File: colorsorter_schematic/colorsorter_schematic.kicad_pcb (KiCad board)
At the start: 2 copper layers, 6 parts, among them U1 PIC24FJ64GA702-I/SO, U2 ESP8266-01_ESP-01

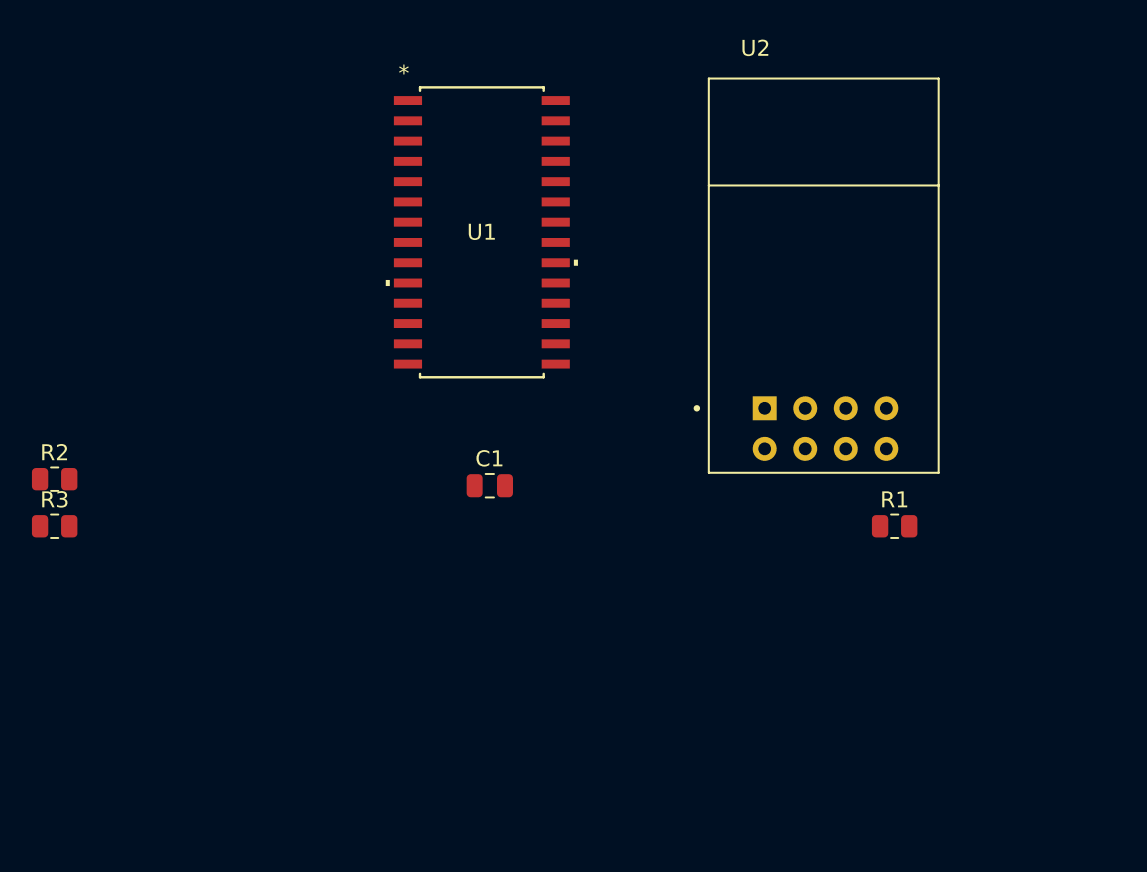
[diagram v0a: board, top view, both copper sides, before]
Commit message: Added voltage regulator, oscillator and bulk capacitors.
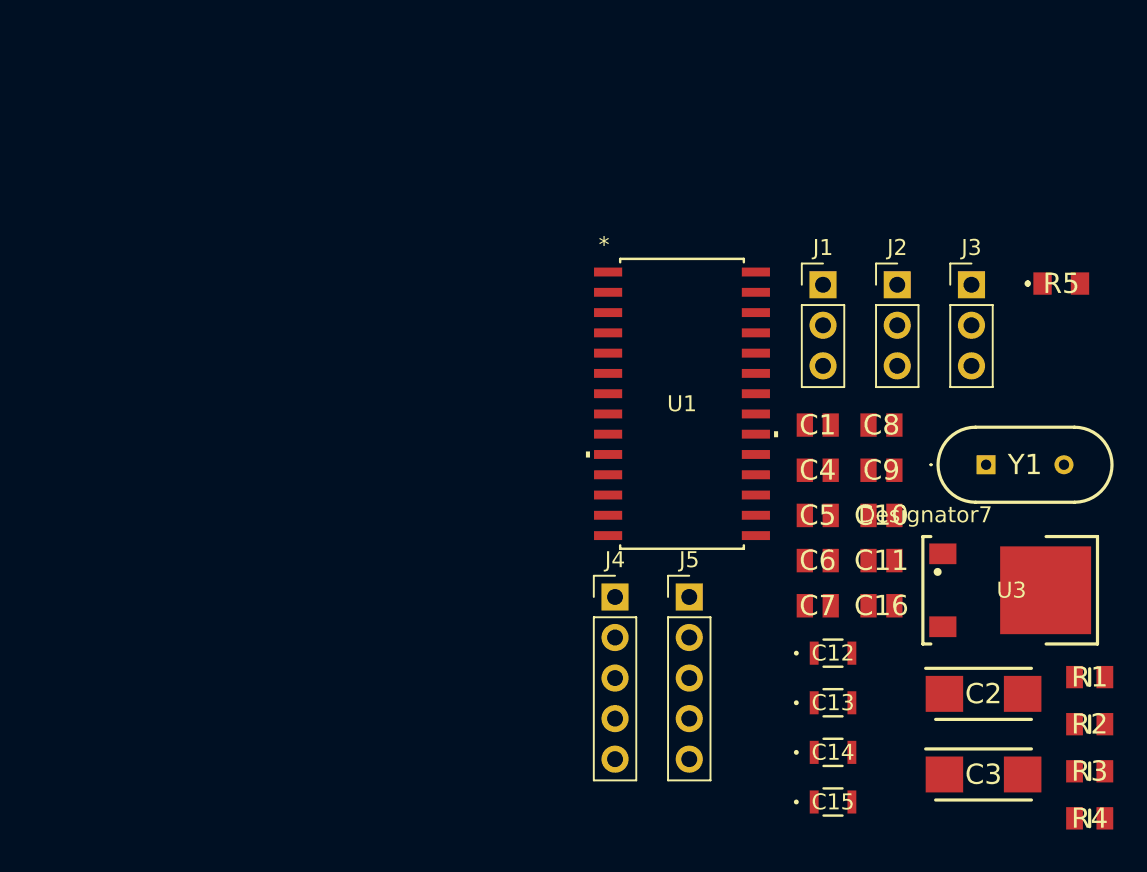
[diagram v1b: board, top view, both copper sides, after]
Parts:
- removed U2: ESP8266-01_ESP-01, ESP8266-01_ESP-01:XCVR_ESP8266-01_ESP-01
- added C10: 0.1u, 0.1uF:CAPC2012X94N, F.Cu at (122.0, 75.5)
- added C11: 0.1u, 0.1uF:CAPC2012X94N, F.Cu at (122.0, 78.3)
- added C12: 10u, 10uF:CAP_2012_TDK, F.Cu at (119.0, 84.1)
- added C13: 10u, 10uF:CAP_2012_TDK, F.Cu at (119.0, 87.3)
- added C14: 10u, 10uF:CAP_2012_TDK, F.Cu at (119.0, 90.4)
- added C15: 10u, 10uF:CAP_2012_TDK, F.Cu at (119.0, 93.5)
- added C16: 0.1u, 0.1uF:CAPC2012X94N, F.Cu at (122.0, 81.2)
- added C2: 10u, 10uFtantalum:CAPPM6032X280N, F.Cu at (128.4, 86.7)
- added C3: 10u, 10uFtantalum:CAPPM6032X280N, F.Cu at (128.4, 91.8)
- added C4: 50p, 50pF:CAPC2012X140N, F.Cu at (118.0, 72.7)
- added C5: 50p, 50pF:CAPC2012X140N, F.Cu at (118.0, 75.5)
- added C6: 0.1u, 0.1uF:CAPC2012X94N, F.Cu at (118.0, 78.3)
- added C7: 0.1u, 0.1uF:CAPC2012X94N, F.Cu at (118.0, 81.2)
- added C8: 0.1u, 0.1uF:CAPC2012X94N, F.Cu at (122.0, 69.9)
- added C9: 0.1u, 0.1uF:CAPC2012X94N, F.Cu at (122.0, 72.7)
- added J1: Conn_01x03_Pin, Connector_PinHeader_2.54mm:PinHeader_1x03_P2.54mm_Vertical, F.Cu at (118.3, 61.1)
- added J2: Conn_01x03_Pin, Connector_PinHeader_2.54mm:PinHeader_1x03_P2.54mm_Vertical, F.Cu at (123.0, 61.1)
- added J3: Conn_01x03_Pin, Connector_PinHeader_2.54mm:PinHeader_1x03_P2.54mm_Vertical, F.Cu at (127.6, 61.1)
- added J4: Conn_01x05_Pin, Connector_PinHeader_2.54mm:PinHeader_1x05_P2.54mm_Vertical, F.Cu at (105.3, 80.6)
- added J5: Conn_01x05_Pin, Connector_PinHeader_2.54mm:PinHeader_1x05_P2.54mm_Vertical, F.Cu at (110.0, 80.6)
- added R4: 10k, 10kohm:RESC2012X70N, F.Cu at (135.1, 94.5)
- added R5: 330, 330ohm:ERJP06D1000V, F.Cu at (133.3, 61.0)
- added U3: LM1117DT-3.3/NOPB, voltageregulator:NDP0003B, F.Cu at (130.2, 80.2)
- added Y1: 830003156B, crystaloscillator:830003156B, F.Cu at (128.6, 72.3)
- C1: value 100n -> 0.1u; footprint capacitor_smd:C_0805_2012Metric -> 0.1uF:CAPC2012X94N
- R1: footprint Resistor_SMD:R_0805_2012Metric -> 10kohm:RESC2012X70N
- R2, R3: value 4.7k -> 10k; footprint Resistor_SMD:R_0805_2012Metric -> 10kohm:RESC2012X70N
- U1: footprint footprints:SOIC28__SO28_MCH -> PIC24FJ64GA702-I-SO:SOIC28__SO28_MCH
- moved R2 66.6 mm to (135.1, 88.6)
- moved R3 66.6 mm to (135.1, 91.5)
- moved C1 20.9 mm to (118.0, 69.9)
- moved U1 16.5 mm to (109.5, 68.5)
- moved R1 15.4 mm to (135.1, 85.7)
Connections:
- C1 pad 1: +3.3V -> Net-(U2-GND)
- C1 pad 2: GND -> +3.3V
- R1 pad 1: Net-(U2-~{RST}) -> +3.3V
- R1 pad 2: +3.3V -> Net-(U2-~{RST})
- R2 pad 1: +3.3V -> Net-(J4-Pin_3)
- R2 pad 2: Net-(SDA1-Pin_1) -> GND
- R3 pad 1: +3.3V -> Net-(J4-Pin_4)
- R3 pad 2: Net-(SCL1-Pin_1) -> GND
- U1 pad 1: unconnected-(U1-*MCLR-Pad1) -> Net-(SW1-B)
- U1 pad 10: unconnected-(U1-OSCO/CLKO/C2IND/RA3-Pad10) -> Net-(U1-OSCO/CLKO/C2IND/RA3)
- U1 pad 13: unconnected-(U1-VDD-Pad13) -> +3.3V
- U1 pad 14: unconnected-(U1-PGD3/RP5/ASDA1/OCM1E/RB5-Pad14) -> Net-(J2-Pin_3)
- U1 pad 17: Net-(SCL1-Pin_1) -> /SCL
- U1 pad 18: Net-(SDA1-Pin_1) -> /SDA
- U1 pad 19: unconnected-(U1-VSS-Pad19) -> GND
- U1 pad 20: unconnected-(U1-VCAP-Pad20) -> Net-(U1-VCAP)
- U1 pad 25: unconnected-(U1-CVREF/AN6/C3INB/RP14/CTED5/RB14-Pad25) -> Net-(J3-Pin_3)
- U1 pad 26: unconnected-(U1-AN9/C3INA/RP15/CTED6/RB15-Pad26) -> Net-(J1-Pin_3)
- U1 pad 27: unconnected-(U1-AVSS/VSS-Pad27) -> GND
- U1 pad 28: unconnected-(U1-AVDD/VDD-Pad28) -> +3.3V
- U1 pad 4: unconnected-(U1-PGD1/AN2/CTCMP/C2INB/RP0/RB0-Pad4) -> Net-(J4-Pin_3)
- U1 pad 5: unconnected-(U1-PGC1/AN1-/AN3/C2INA/RP1/CTED12/RB1-Pad5) -> Net-(J4-Pin_4)
- U1 pad 8: unconnected-(U1-VSS-Pad8) -> GND
- U1 pad 9: unconnected-(U1-OSCI/CLKI/C1IND/RA2-Pad9) -> Net-(U1-OSCI/CLKI/C1IND/RA2)

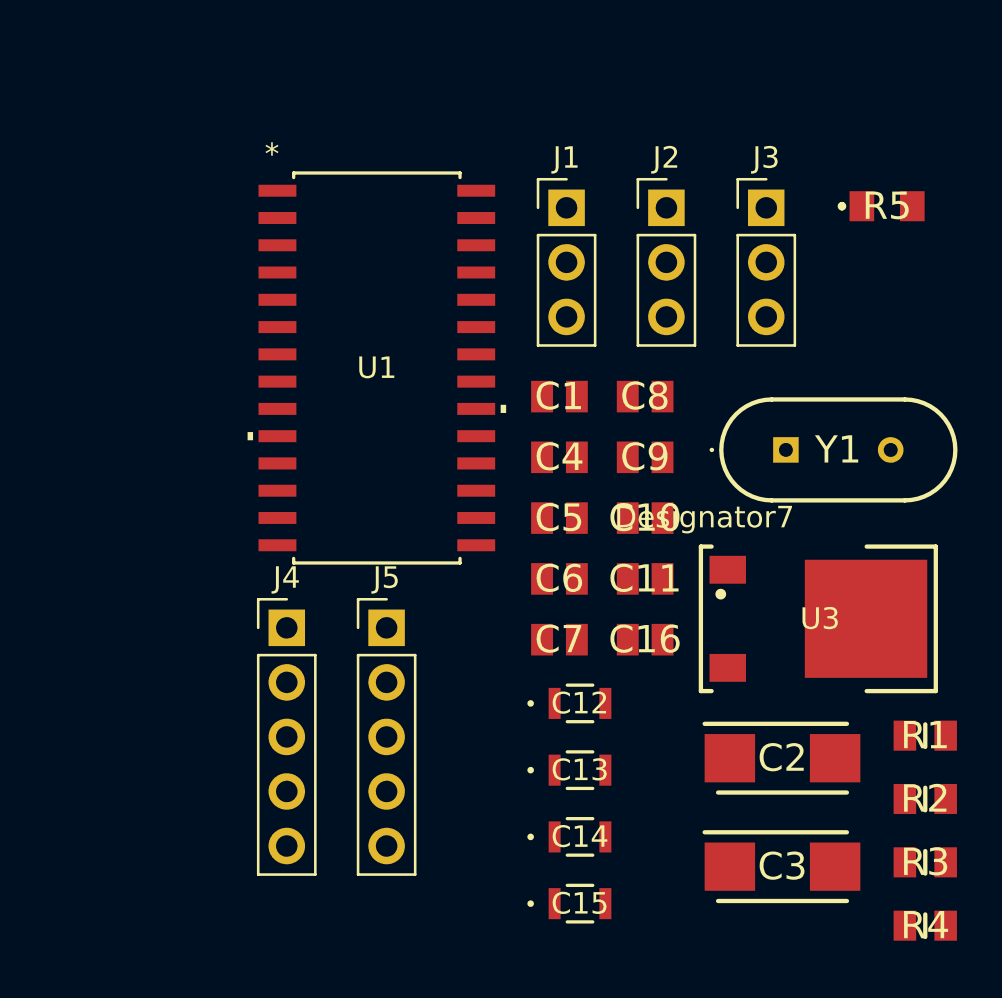
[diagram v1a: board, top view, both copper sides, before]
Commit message: Added additional pins header.
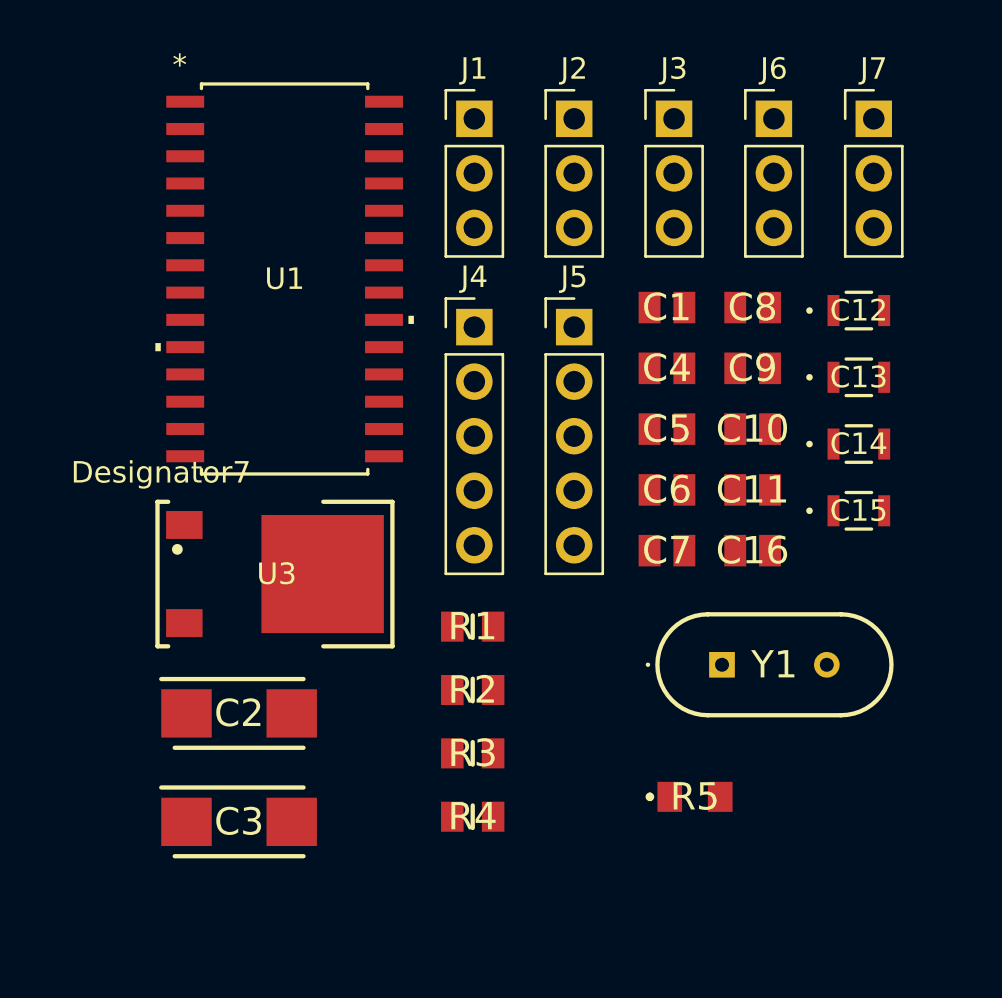
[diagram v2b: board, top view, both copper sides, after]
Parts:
- added J6: Conn_01x03_Pin, Connector_PinHeader_2.54mm:PinHeader_1x03_P2.54mm_Vertical, F.Cu at (128.0, 56.9)
- added J7: Conn_01x03_Pin, Connector_PinHeader_2.54mm:PinHeader_1x03_P2.54mm_Vertical, F.Cu at (132.7, 56.9)
- moved R5 28.9 mm to (124.3, 88.5)
- moved C2 25.4 mm to (103.1, 84.6)
- moved C3 25.4 mm to (103.1, 89.7)
- moved U3 25.4 mm to (104.8, 78.1)
- moved C12 22.4 mm to (132.0, 65.9)
- moved C13 22.4 mm to (132.0, 69.0)
- moved C14 22.4 mm to (132.0, 72.1)
- moved C15 22.4 mm to (132.0, 75.2)
- moved R1 21.7 mm to (114.0, 80.6)
- moved R3 21.7 mm to (114.0, 86.5)
- moved R4 21.7 mm to (114.0, 89.4)
- moved R2 21.7 mm to (114.0, 83.5)
- moved J4 16.5 mm to (114.0, 66.6)
- moved J5 16.5 mm to (118.7, 66.6)
- moved Y1 10.4 mm to (125.6, 82.3)
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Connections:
- C1 pad 1: Net-(U2-GND) -> GND
- U1 pad 11: unconnected-(U1-SOSCI/RP4/RB4-Pad11) -> Net-(J7-Pin_3)
- U1 pad 22: unconnected-(U1-PGC2/TMS/REFI1/RP11/CTED9/RB11-Pad22) -> Net-(J6-Pin_3)
- U1 pad 23: unconnected-(U1-AN8/LVDIN/RP12/RB12-Pad23) -> Net-(J6-Pin_2)
- U1 pad 24: unconnected-(U1-AN7/C1INC/RP13/OCM1D/CTPLS/RB13-Pad24) -> Net-(J6-Pin_1)
- U1 pad 6: unconnected-(U1-AN4/C1INB/RP2/SDA2/CTED13/RB2-Pad6) -> Net-(J7-Pin_1)
- U1 pad 7: unconnected-(U1-AN5/C1INA/RP3/SCL2/CTED8/RB3-Pad7) -> Net-(J7-Pin_2)

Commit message: Dodavanje izmjena u semi i rutranje na pcb
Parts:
- added Power: PinHeader_1x02_P2.54mm_Vertical, Connector_PinHeader_2.54mm:PinHeader_1x02_P2.54mm_Vertical, F.Cu at (61.0, 86.4)
- added REF**: XCVR_ESP8266-01_ESP-01, ESP8266-01_ESP-01 FOOTPRINT:XCVR_ESP8266-01_ESP-01, F.Cu at (122.9, 91.9)
- added S**: SLW12768644AD, SwitcH:SLW12768644AD, F.Cu at (77.5, 44.8)
- moved R5 68.0 mm to (68.6, 49.5)
- moved R4 66.6 mm to (63.5, 46.0), turned to -90 degrees
- moved C6 63.5 mm to (63.5, 52.1), turned to 90 degrees
- moved C7 53.4 mm to (72.0, 92.7)
- moved J4 50.7 mm to (63.5, 62.2)
- moved R3 45.8 mm to (70.8, 71.1)
- moved R2 45.8 mm to (71.1, 67.3)
- moved C4 44.6 mm to (78.5, 66.3), turned to 180 degrees
- moved C5 44.1 mm to (78.9, 70.0), turned to 180 degrees
- moved C14 43.8 mm to (88.9, 80.2), turned to 90 degrees
- moved C8 43.3 mm to (90.2, 88.4), turned to 90 degrees
- moved Y1 42.6 mm to (84.8, 70.0), turned to 90 degrees
- moved C9 38.8 mm to (88.9, 76.0), turned to 90 degrees
- moved J7 38.4 mm to (95.3, 48.3), turned to 90 degrees
- moved C1 36.5 mm to (105.6, 97.8), turned to 180 degrees
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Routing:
- net GND: track 0.00 -> 39.6 mm, vias 0 -> 2
- net +3.3V: track 0.00 -> 35.5 mm
- net (no net): track 0.00 -> 32.9 mm
- net Net-(J6-Pin_1): track 0.00 -> 20.7 mm
- net Net-(J6-Pin_2): track 0.00 -> 17.9 mm
- net Net-(J7-Pin_2): track 0.00 -> 17.8 mm
- net Net-(SW1-B): track 0.00 -> 14.5 mm
- net Net-(U1-OSCI/CLKI/C1IND/RA2): track 0.00 -> 14.0 mm
- net Net-(J6-Pin_3): track 0.00 -> 14.0 mm
- net Net-(SW1-A): track 0.00 -> 9.59 mm
- net +4.5V: track 0.00 -> 8.65 mm
- net Net-(C6-Pad2): track 0.00 -> 8.49 mm
- net Net-(J4-Pin_4): track 0.00 -> 8.40 mm
- net Net-(U1-OSCO/CLKO/C2IND/RA3): track 0.00 -> 7.04 mm
- net Net-(U1-VCAP): track 0.00 -> 3.78 mm
- added copper zone on B.Cu, net GND

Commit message: Updated schematic and pcb.
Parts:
- removed Power: PinHeader_1x02_P2.54mm_Vertical, Connector_PinHeader_2.54mm:PinHeader_1x02_P2.54mm_Vertical
- removed REF**: XCVR_ESP8266-01_ESP-01, ESP8266-01_ESP-01 FOOTPRINT:XCVR_ESP8266-01_ESP-01
- removed S**: SLW12768644AD, SwitcH:SLW12768644AD
- added J8: Conn_01x02_Pin, Connector_PinHeader_2.54mm:PinHeader_1x02_P2.54mm_Vertical, F.Cu at (166.1, 97.1)
- added SW1: SW_SPDT, twostateswitch:SLW12768644AD, F.Cu at (145.9, 107.5)
- added U2: ESP8266-01_ESP-01, wifi:wifi, F.Cu at (134.9, 86.4)
- U3: footprint voltageregulator:NDP0003B -> NDP0003B:NDP0003B
- moved R4 112.8 mm to (166.0, 93.3), turned to 0 degrees
- moved J4 106.3 mm to (160.8, 104.8)
- moved R5 103.3 mm to (159.1, 99.4)
- moved C6 102.7 mm to (157.8, 92.9), turned to 0 degrees
- moved R3 97.1 mm to (166.0, 90.3)
- moved R2 97.0 mm to (166.0, 87.4)
- moved C7 85.8 mm to (157.8, 95.7)
- moved C4 82.0 mm to (157.8, 87.2), turned to 0 degrees
- moved C5 81.3 mm to (157.8, 90.0), turned to 0 degrees
- moved Y1 77.7 mm to (147.3, 116.3), turned to 0 degrees
- moved C9 73.7 mm to (161.7, 87.2), turned to 0 degrees
- moved J7 73.6 mm to (163.7, 75.6), turned to 0 degrees
- moved C8 71.7 mm to (161.7, 84.4), turned to 0 degrees
- moved C10 66.9 mm to (161.7, 90.0), turned to 0 degrees
- moved C13 66.6 mm to (137.9, 112.1)
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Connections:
- net +3.3V renamed Net-(C3-+)
- net +4.5V renamed Net-(C2-+)
- Y1 pad 1: (no net) -> Net-(U1-OSCO/CLKO/C2IND/RA3)
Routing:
- net GND: track 39.6 -> 0.00 mm, vias 2 -> 0
- net Net-(C3-+): track 35.5 -> 0.00 mm
- net (no net): track 32.9 -> 0.00 mm
- net Net-(J6-Pin_1): track 20.7 -> 0.00 mm
- net Net-(J6-Pin_2): track 17.9 -> 0.00 mm
- net Net-(J7-Pin_2): track 17.8 -> 0.00 mm
- net Net-(SW1-B): track 14.5 -> 0.00 mm
- net Net-(U1-OSCI/CLKI/C1IND/RA2): track 14.0 -> 0.00 mm
- net Net-(J6-Pin_3): track 14.0 -> 0.00 mm
- net Net-(SW1-A): track 9.59 -> 0.00 mm
- net Net-(C2-+): track 8.65 -> 0.00 mm
- net Net-(C6-Pad2): track 8.49 -> 0.00 mm
- net Net-(J4-Pin_4): track 8.40 -> 0.00 mm
- net Net-(U1-OSCO/CLKO/C2IND/RA3): track 7.04 -> 0.00 mm
- net Net-(U1-VCAP): track 3.78 -> 0.00 mm
- removed copper zone on B.Cu, net GND

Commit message: Schematics Updated 15/1/2025
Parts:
- moved Power 53.9 mm to (114.3, 112.1), turned to 180 degrees
- moved R4 52.5 mm to (114.3, 84.2), turned to 90 degrees
- moved U2 51.5 mm to (165.1, 128.1), turned to 180 degrees
- moved J4 48.3 mm to (114.3, 91.8)
- moved R5 48.1 mm to (115.5, 79.1)
- moved R3 46.5 mm to (120.7, 100.7), turned to -90 degrees
- moved R2 46.1 mm to (120.7, 95.6), turned to 90 degrees
- moved C6 41.2 mm to (116.8, 88.0), turned to 90 degrees
- moved C7 39.8 mm to (127.0, 121.0), turned to 180 degrees
- moved C13 37.7 mm to (161.7, 82.9)
- moved SW1 36.3 mm to (123.2, 79.1), turned to -90 degrees
- moved C8 35.8 mm to (139.7, 112.6), turned to 90 degrees
- moved J2 34.0 mm to (151.1, 109.6), turned to -90 degrees
- moved C15 32.9 mm to (161.7, 95.6)
- moved J1 30.6 mm to (175.2, 80.4), turned to -90 degrees
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- renumbered J8 to Power
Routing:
- net Net-(C3-+): track 0.00 -> 197.4 mm, vias 0 -> 6
- net Net-(C2-+): track 0.00 -> 147.8 mm
- net GND: track 0.00 -> 90.6 mm, vias 0 -> 23
- net Net-(U1-RP7/OCM1A/CTED3/INT0/RB7): track 0.00 -> 46.5 mm
- net Net-(J4-Pin_4): track 0.00 -> 40.1 mm
- net Net-(J4-Pin_3): track 0.00 -> 39.3 mm
- net Net-(U1-OSCI/CLKI/C1IND/RA2): track 0.00 -> 27.8 mm
- net Net-(SW1-B): track 0.00 -> 23.6 mm
- net Net-(U1-PGC3/RP6/ASCL1/OCM1F/RB6): track 0.00 -> 22.8 mm
- net Net-(J7-Pin_3): track 0.00 -> 22.8 mm
- net Net-(J6-Pin_1): track 0.00 -> 21.0 mm
- net Net-(U1-OSCO/CLKO/C2IND/RA3): track 0.00 -> 19.9 mm, vias 0 -> 2
- net /SCL: track 0.00 -> 19.8 mm
- net Net-(J6-Pin_2): track 0.00 -> 18.0 mm
- net Net-(J1-Pin_3): track 0.00 -> 17.9 mm
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
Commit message: Popravljena verzija pcb-a.
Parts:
- moved C5 2.15 mm to (138.9, 93.5)
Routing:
- net Net-(U1-OSCO/CLKO/C2IND/RA3): track 19.9 -> 17.9 mm
- net Net-(C3-+): track 197.4 -> 198.7 mm
- net GND: track 90.6 -> 89.4 mm
